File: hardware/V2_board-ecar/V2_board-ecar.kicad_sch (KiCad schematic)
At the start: 89 parts, among them IC1 ATMEGA8A-P, J1 2x BATT IN, J10 24V, J11 18V, J12 5V, J13 Analog-in-2 0-5V, J14 IGBT, J15 Analog-in-3 - 30to5 (batt), J16 Mosfet Out (Fan), J17 2x Switch (to 5V), J18 Relay contacts, J2 ST 2x GND, J3 2x 24V filtered, J4 ST 2x GND, J5 PWM-Signal, J6 LED ~3,2V 20mA, J7 Gas Pedal, J8 Gate, J9 BATT, K1 LEG-5, P1 ISP, Q1 BC547, Q2 IRFZ24N, Q3 BC547, U1 LM7818CT, U2 LM2576T-5, U3 TC429

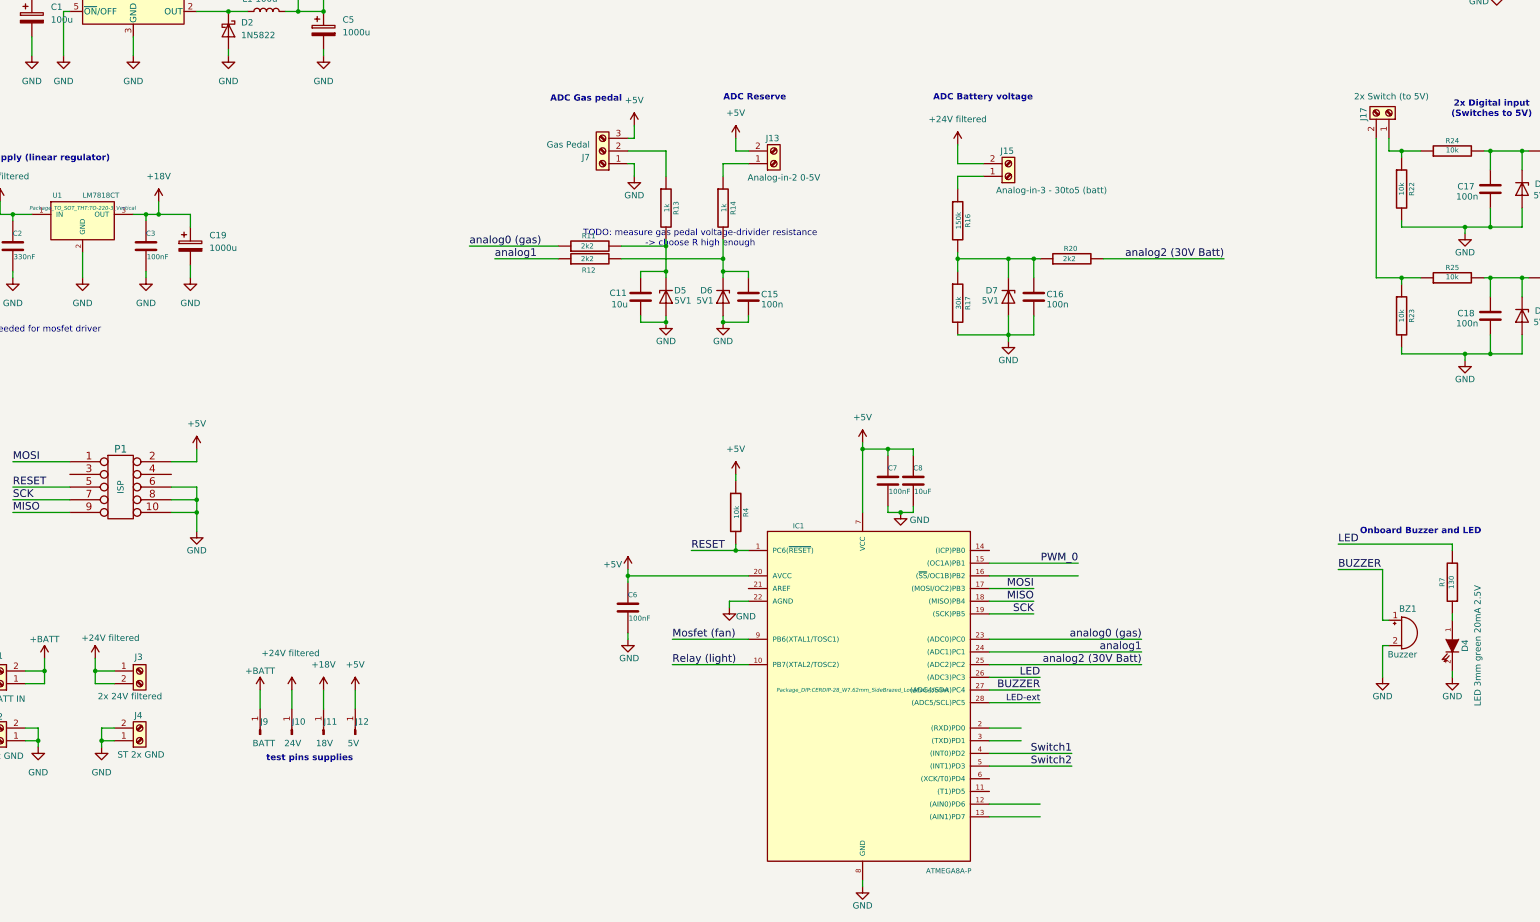
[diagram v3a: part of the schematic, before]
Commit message: pcb: start layout, arrange components by schematic
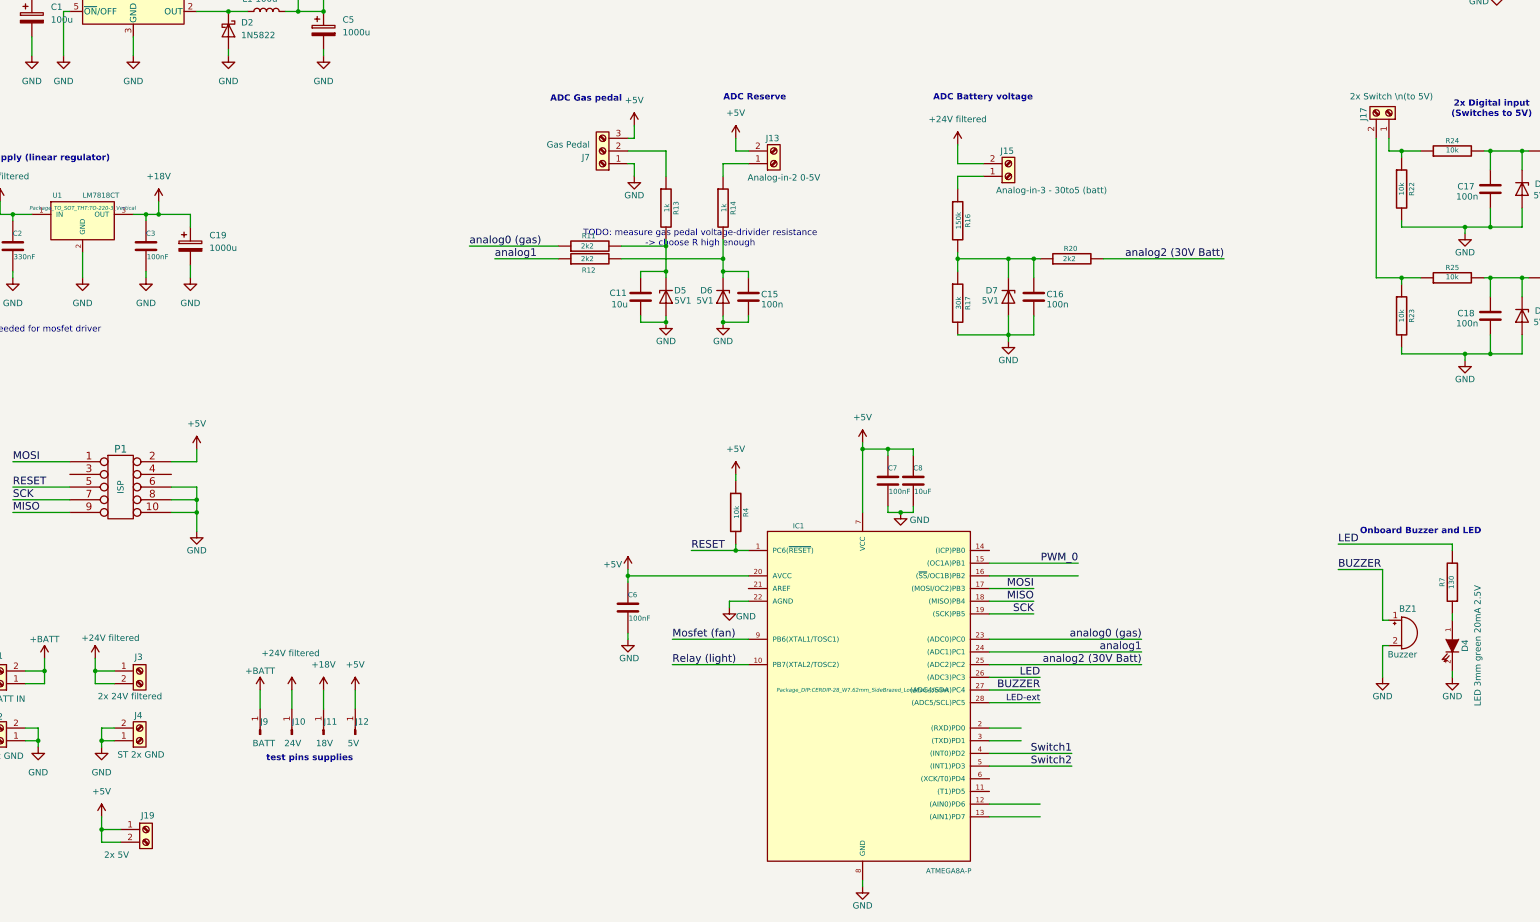
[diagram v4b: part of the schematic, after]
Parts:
- added J19: 2x 5V, TerminalBlock:TerminalBlock_bornier-2_P5.08mm, symbol Connector:Screw_Terminal_01x02
- J17: value 2x Switch (to 5V) -> 2x Switch \n(to 5V)
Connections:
- net +5V: now also J19.1 (Pin_1), J19.2 (Pin_2)
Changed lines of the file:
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@@
 	)
 	(junction
+		(at 45.72 247.65)
+		(diameter 0)
+		(color 0 0 0 0)
+	)
+	(junction
 		(at 252.73 53.34)
 		(diameter 0)
@@
 	(wire
 		(pts
+			(xy 49.53 250.19) (xy 45.72 250.19)
+		)
+		(stroke
+			(width 0)
+			(type default)
+		)
+	)
+	(wire
+		(pts
 			(xy 217.17 114.3) (xy 217.17 110.49)
 		)
@@
 	(wire
 		(pts
+			(xy 45.72 250.19) (xy 45.72 247.65)
+		)
+		(stroke
+			(width 0)
+			(type default)
+		)
+	)
+	(wire
+		(pts
 			(xy 153.67 146.05) (xy 158.75 146.05)
 		)
@@
 	(wire
 		(pts
+			(xy 45.72 247.65) (xy 49.53 247.65)
+		)
+		(stroke
+			(width 0)
+			(type default)
+		)
+	)
+	(wire
+		(pts
 			(xy 73.66 44.45) (xy 73.66 49.53)
 		)
@@
 	(wire
 		(pts
+			(xy 45.72 245.11) (xy 45.72 247.65)
+		)
+		(stroke
+			(width 0)
+			(type default)
+		)
+	)
+	(wire
+		(pts
 			(xy 31.75 78.74) (xy 31.75 81.28)
 		)
@@
 	)
 	(symbol
+		(lib_id "power:+5V")
+		(at 45.72 245.11 0)
+		(unit 1)
+		(exclude_from_sim no)
+		(in_bom yes)
+		(on_board yes)
+		(dnp no)
+		(fields_autoplaced yes)
+		(property "Reference" "#PWR062"
+			(at 45.72 248.92 0)
+			(effects
+				(font
+					(size 1.27 1.27)
+				)
+				(hide yes)
+			)
+		)
+		(property "Value" "+5V"
+			(at 45.72 240.03 0)
+			(effects
+				(font
+					(size 1.27 1.27)
+				)
+			)
+		)
+		(property "Footprint" ""
+			(at 45.72 245.11 0)
+			(effects
+				(font
+					(size 1.27 1.27)
+				)
+				(hide yes)
+			)
+		)
+		(property "Datasheet" ""
+			(at 45.72 245.11 0)
+			(effects
+				(font
+					(size 1.27 1.27)
+				)
+				(hide yes)
+			)
+		)
+		(property "Description" "Power symbol creates a global label with name \"+5V\""
+			(at 45.72 245.11 0)
+			(effects
+				(font
+					(size 1.27 1.27)
+				)
+				(hide yes)
+			)
+		)
+		(pin "1"
+		)
+		(instances
+			(project "V2_board-ecar"
+				(path "/5b898ce7-7cb2-4d45-8284-d2f49c9d3242"
+					(reference "#PWR062")
+					(unit 1)
+				)
+			)
+		)
+	)
+	(symbol
 		(lib_id "control-rescue:R")
 		(at 316.23 198.12 180)
@@
 			)
 		)
-		(property "Value" "2x  Switch (to 5V)"
+		(property "Value" "2x  Switch \\n(to 5V)"
 			(at 304.038 100.838 90)
 			(effects
@@
 					(unit 1)
 				)
+			)
+		)
+	)
+	(symbol
+		(lib_id "Connector:Screw_Terminal_01x02")
+		(at 54.61 247.65 0)
+		(unit 1)
+		(exclude_from_sim no)
+		(in_bom yes)
+		(on_board yes)
+		(dnp no)
+		(property "Reference" "J19"
+			(at 53.594 244.856 0)
+			(effects
+				(font
+					(size 1.27 1.27)
+				)
+				(justify left)
+			)
+		)
+		(property "Value" "2x 5V"
+			(at 46.228 252.73 0)
+			(effects
+				(font
+					(size 1.27 1.27)
+				)
+				(justify left)
+			)
+		)
+		(property "Footprint" "TerminalBlock:TerminalBlock_bornier-2_P5.08mm"
+			(at 54.61 247.65 0)
+			(effects
+				(font
+					(size 1.27 1.27)
+				)
+				(hide yes)
+			)
+		)
+		(property "Datasheet" "~"
+			(at 54.61 247.65 0)
+			(effects
+				(font
+					(size 1.27 1.27)
+				)
+				(hide yes)
+			)
+		)
+		(property "Description" "Generic screw terminal, single row, 01x02, script generated (kicad-library-utils/schlib/autogen/connector/)"
+			(at 54.61 247.65 0)
+			(effects
+				(font
+					(size 1.27 1.27)
+				)
+				(hide yes)
+			)
+		)
+		(pin "2"
+		)
+		(pin "1"
+		)
+		(instances
+			(project "V2_board-ecar"
+				(path "/5b898ce7-7cb2-4d45-8284-d2f49c9d3242"
+					(reference "J19")
+					(unit 1)
+				)

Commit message: pcb: placed all parts
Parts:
- removed D8: D, Diode_THT:D_T-1_P12.70mm_Horizontal, symbol Device:D
- removed R2: nopop, Resistor_THT:R_Axial_DIN0922_L20.0mm_D9.0mm_P25.40mm_Horizontal, symbol Device:R
- added J20: ADC Battery, Connector_PinHeader_1.00mm:PinHeader_1x01_P1.00mm_Vertical, symbol Connector:Conn_01x01_Pin
- added J21: ADC reserve, Connector_PinHeader_1.00mm:PinHeader_1x01_P1.00mm_Vertical, symbol Connector:Conn_01x01_Pin
- added J22: ADC Gas-pedal, Connector_PinHeader_1.00mm:PinHeader_1x01_P1.00mm_Vertical, symbol Connector:Conn_01x01_Pin
- J17: value 2x Switch \n(to 5V) -> 2x Switch (to 5V)
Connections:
- net GND: now also J14.1 (Pin_1); no longer J14.2 (Pin_2)
- net at C16.1, D7.1 (K), R16.2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: now also J20.1 (Pin_1)
- net at J8.1 (Pin_1), U3.6 (OUT), U3.7 (OUT): now also J14.2 (Pin_2); no longer J14.1 (Pin_1)
- net at C11.1, D5.1 (K), R11.2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: now also J22.1 (Pin_1)
- net at C15.1, D6.1 (K), R12.2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: now also J21.1 (Pin_1)
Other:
- moved on the sheet: C11, D5, J14, J7, R11, R12, R13

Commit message: pcb: Add moutingholes, fuses
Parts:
- removed D10: D, Diode_THT:D_T-1_P12.70mm_Horizontal, symbol Device:D
- added F2, F3, F4: 500mA, Fuse:Fuseholder_Cylinder-5x20mm_Stelvio-Kontek_PTF78_Horizontal_Open, symbol Device:Fuse
- added H1, H2, H3, H4: MountingHole, MountingHole:MountingHole_5.3mm_M5, symbol Mechanical:MountingHole
- J16: value Mosfet Out (Fan) -> Mosfet Out (Diode, Mosfet)
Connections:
- net +24V filtered: now also F2.2; no longer C10.1, C4.1, C9.1, D1.1 (K), D3.2 (A2), D9.1 (K), J16.2 (Pin_2), R3.2
- net at D9.2 (A), J16.1 (Pin_1): now also F4.2; no longer Q2.2 (D)
- net at K1.1: now also F3.1; no longer J18.2 (Pin_2)
- new net: D9.1 (K), J16.2 (Pin_2)
- new net: C10.1, C4.1, C9.1, D1.1 (K), D3.2 (A2), F2.1, R3.2
- new net: F3.2, J18.2 (Pin_2)
- new net: F4.1, Q2.2 (D)
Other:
- note removed: "populate diodes depending on where load is connected"
- moved on the sheet: D9, J16

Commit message: pcb: layout complete (for review)
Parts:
- added J23: 2x 24V filtered, TerminalBlock:TerminalBlock_bornier-2_P5.08mm, symbol Connector:Screw_Terminal_01x02
- added R2: 10, Resistor_THT:R_Axial_DIN0207_L6.3mm_D2.5mm_P10.16mm_Horizontal, symbol control-rescue:R
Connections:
- net +24V filtered: now also J23.1 (Pin_1), J23.2 (Pin_2); no longer J15.2 (Pin_2)
- net +5V: now also J15.2 (Pin_2)
- net BUZZER: now also R2.2; no longer BZ1.1 (+)
- net Mosfet (fan): now also IC1.16 ((~{SS}/OC1B)PB2); no longer IC1.9 (PB6(XTAL1/TOSC1))
- net analog0 (gas): now also IC1.25 ((ADC2)PC2); no longer IC1.23 ((ADC0)PC0)
- net analog2 (30V Batt): now also IC1.23 ((ADC0)PC0); no longer IC1.25 ((ADC2)PC2)
- new net: BZ1.1 (+), R2.1
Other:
- moved on the sheet: BZ1, J19, J4

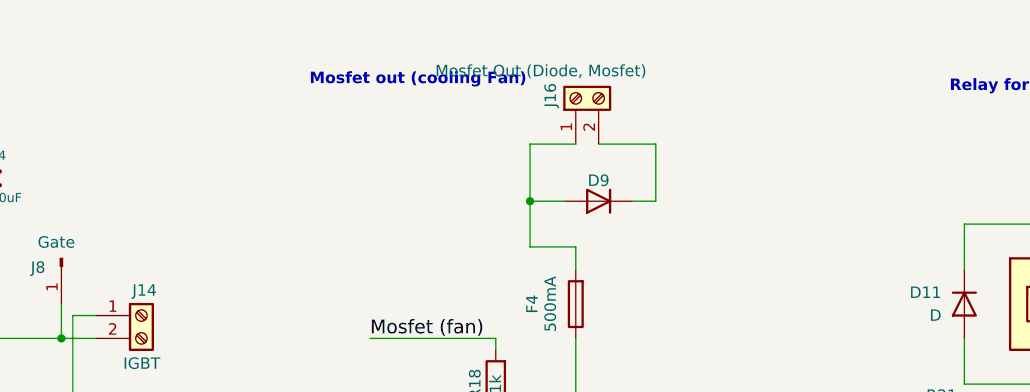
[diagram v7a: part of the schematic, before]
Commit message: pcb: minor optimizations, swap layers
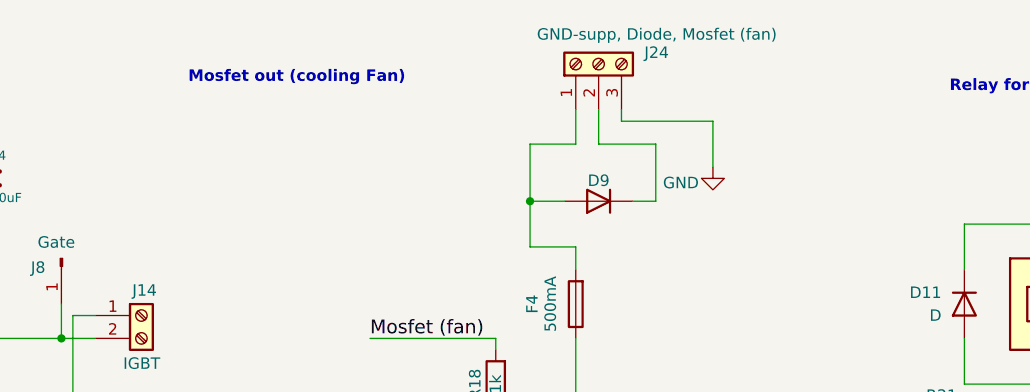
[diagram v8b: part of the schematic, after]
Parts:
- removed J16: Mosfet Out (Diode, Mosfet), TerminalBlock:TerminalBlock_bornier-2_P5.08mm, symbol Connector:Screw_Terminal_01x02
- added J24: GND-supp, Diode, Mosfet (fan), TerminalBlock:TerminalBlock_bornier-3_P5.08mm, symbol Connector:Screw_Terminal_01x03
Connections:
- net GND: now also J24.3 (Pin_3)
- net at D9.1 (K): now also J24.2 (Pin_2)
- net at D9.2 (A), F4.2: now also J24.1 (Pin_1)
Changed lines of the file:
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@@
 	(wire
 		(pts
+			(xy 330.2 29.21) (xy 330.2 27.94)
+		)
+		(stroke
+			(width 0)
+			(type default)
+		)
+	)
+	(wire
+		(pts
 			(xy 138.43 135.89) (xy 147.32 135.89)
 		)
@@
 	(wire
 		(pts
+			(xy 327.66 27.94) (xy 327.66 31.75)
+		)
+		(stroke
+			(width 0)
+			(type default)
+		)
+	)
+	(wire
+		(pts
 			(xy 170.18 135.89) (xy 170.18 137.16)
 		)
@@
 	(wire
 		(pts
+			(xy 325.12 27.94) (xy 325.12 31.75)
+		)
+		(stroke
+			(width 0)
+			(type default)
+		)
+	)
+	(wire
+		(pts
 			(xy 34.29 215.9) (xy 30.48 215.9)
 		)
@@
 	(wire
 		(pts
+			(xy 340.36 29.21) (xy 330.2 29.21)
+		)
+		(stroke
+			(width 0)
+			(type default)
+		)
+	)
+	(wire
+		(pts
 			(xy 391.16 36.83) (xy 391.16 41.91)
 		)
@@
 	(wire
 		(pts
+			(xy 340.36 34.29) (xy 340.36 29.21)
+		)
+		(stroke
+			(width 0)
+			(type default)
+		)
+	)
+	(wire
+		(pts
 			(xy 300.99 109.22) (xy 300.99 137.16)
 		)
@@
 	(text "Mosfet out (cooling Fan)"
 		(exclude_from_sim no)
-		(at 307.594 24.638 0)
+		(at 294.132 24.384 0)
 		(effects
 			(font
@@
 	(symbol
 		(lib_id "power:GND")
+		(at 340.36 34.29 0)
+		(mirror y)
+		(unit 1)
+		(exclude_from_sim no)
+		(in_bom yes)
+		(on_board yes)
+		(dnp no)
+		(property "Reference" "#PWR045"
+			(at 340.36 40.64 0)
+			(effects
+				(font
+					(size 1.27 1.27)
+				)
+				(hide yes)
+			)
+		)
+		(property "Value" "GND"
+			(at 336.804 36.068 0)
+			(effects
+				(font
+					(size 1.27 1.27)
+				)
+			)
+		)
+		(property "Footprint" ""
+			(at 340.36 34.29 0)
+			(effects
+				(font
+					(size 1.27 1.27)
+				)
+				(hide yes)
+			)
+		)
+		(property "Datasheet" ""
+			(at 340.36 34.29 0)
+			(effects
+				(font
+					(size 1.27 1.27)
+				)
+				(hide yes)
+			)
+		)
+		(property "Description" "Power symbol creates a global label with name \"GND\" , ground"
+			(at 340.36 34.29 0)
+			(effects
+				(font
+					(size 1.27 1.27)
+				)
+				(hide yes)
+			)
+		)
+		(pin "1"
+		)
+		(instances
+			(project "V2_board-ecar"
+				(path "/5b898ce7-7cb2-4d45-8284-d2f49c9d3242"
+					(reference "#PWR045")
+					(unit 1)
+				)
+			)
+		)
+	)
+	(symbol
+		(lib_id "power:GND")
 		(at 146.05 116.84 0)
 		(unit 1)
@@
 	)
 	(symbol
+		(lib_id "Connector:Screw_Terminal_01x03")
+		(at 327.66 22.86 90)
+		(unit 1)
+		(exclude_from_sim no)
+		(in_bom yes)
+		(on_board yes)
+		(dnp no)
+		(property "Reference" "J24"
+			(at 332.74 21.5899 90)
+			(effects
+				(font
+					(size 1.27 1.27)
+				)
+				(justify right)
+			)
+		)
+		(property "Value" "GND-supp, Diode, Mosfet (fan)"
+			(at 320.802 19.558 90)
+			(effects
+				(font
+					(size 1.27 1.27)
+				)
+				(justify right)
+			)
+		)
+		(property "Footprint" "TerminalBlock:TerminalBlock_bornier-3_P5.08mm"
+			(at 327.66 22.86 0)
+			(effects
+				(font
+					(size 1.27 1.27)
+				)
+				(hide yes)
+			)
+		)
+		(property "Datasheet" "~"
+			(at 327.66 22.86 0)
+			(effects
+				(font
+					(size 1.27 1.27)
+				)
+				(hide yes)
+			)
+		)
+		(property "Description" "Generic screw terminal, single row, 01x03, script generated (kicad-library-utils/schlib/autogen/connector/)"
+			(at 327.66 22.86 0)
+			(effects
+				(font
+					(size 1.27 1.27)
+				)
+				(hide yes)
+			)
+		)
+		(pin "1"
+		)
+		(pin "3"
+		)
+		(pin "2"
+		)
+		(instances
+			(project "V2_board-ecar"
+				(path "/5b898ce7-7cb2-4d45-8284-d2f49c9d3242"
+					(reference "J24")
+					(unit 1)
+				)
+			)
+		)
+	)
+	(symbol
 		(lib_id "treiber-rescue:C")
 		(at 54.61 130.81 0)
@@
 					(unit 1)
 				)
-			)
-		)
-	)
-	(symbol
-		(lib_id "Connector:Screw_Terminal_01x02")
-		(at 325.12 26.67 90)
-		(unit 1)
-		(exclude_from_sim no)
-		(in_bom yes)
-		(on_board yes)
-		(dnp no)
-		(property "Reference" "J16"
-			(at 322.326 27.686 0)
-			(effects
-				(font
-					(size 1.27 1.27)
-				)
-				(justify left)
-			)
-		)
-		(property "Value" "Mosfet Out (Diode, Mosfet)"
-			(at 332.994 23.622 90)
-			(effects
-				(font
-					(size 1.27 1.27)
-				)
-				(justify left)
-			)
-		)
-		(property "Footprint" "TerminalBlock:TerminalBlock_bornier-2_P5.08mm"
-			(at 325.12 26.67 0)
-			(effects
-				(font
-					(size 1.27 1.27)
-				)
-				(hide yes)
-			)
-		)
-		(property "Datasheet" "~"
-			(at 325.12 26.67 0)
-			(effects
-				(font
-					(size 1.27 1.27)
-				)
-				(hide yes)
-			)
-		)
-		(property "Description" "Generic screw terminal, single row, 01x02, script generated (kicad-library-utils/schlib/autogen/connector/)"
-			(at 325.12 26.67 0)
-			(effects
-				(font
-					(size 1.27 1.27)
-				)
-				(hide yes)
-			)
-		)
-		(pin "2"
-		)
-		(pin "1"
-		)
-		(instances
-			(project "V2_board-ecar"
-				(path "/5b898ce7-7cb2-4d45-8284-d2f49c9d3242"
-					(reference "J16")
-					(unit 1)
-				)
